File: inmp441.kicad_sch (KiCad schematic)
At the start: 9 parts

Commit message: Revert PWR_FLAG additions - remove '??' squares from schematics
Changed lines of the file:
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@@
-		)
-	)
-	(symbol
-		(lib_id "power:PWR_FLAG")
-		(at 50.0 50.0 0)
-		(unit 1)
-		(body_style 1)
-		(exclude_from_sim no)
-		(in_bom no)
-		(on_board yes)
-		(in_pos_files no)
-		(dnp no)
-		(property "Reference" "#FLG040"
-			(at 50.0 45.0 0)
-			(hide yes)
-			(show_name no)
-			(do_not_autoplace no)
-			(effects
-				(font
-					(size 1.27 1.27)
-				)
-			)
-		)
-		(property "Value" "PWR_FLAG"
-			(at 50.0 55.0 0)
-			(hide yes)
-			(show_name no)
-			(do_not_autoplace no)
-			(effects
-				(font
-					(size 1.27 1.27)
-				)
-			)
-		)
-		(pin "1"
-			(uuid "e3f4a5b6-7890-12cd-ef01-234567890123-pin1")
-		)
-		(instances
-			(project "esp32_xiaozhi"
-				(path "/cae338e8-f342-43cb-b99a-a0486629133c/d2e61921-5974-44e2-9221-de7c05f17e70"
-					(reference "#FLG040")
-					(unit 1)
-				)
-			)
-		)
-	)
-	(symbol
-		(lib_id "power:PWR_FLAG")
-		(at 50.0 100.0 0)
-		(unit 1)
-		(body_style 1)
-		(exclude_from_sim no)
-		(in_bom no)
-		(on_board yes)
-		(in_pos_files no)
-		(dnp no)
-		(property "Reference" "#FLG041"
-			(at 50.0 95.0 0)
-			(hide yes)
-			(show_name no)
-			(do_not_autoplace no)
-			(effects
-				(font
-					(size 1.27 1.27)
-				)
-			)
-		)
-		(property "Value" "PWR_FLAG"
-			(at 50.0 105.0 0)
-			(hide yes)
-			(show_name no)
-			(do_not_autoplace no)
-			(effects
-				(font
-					(size 1.27 1.27)
-				)
-			)
-		)
-		(pin "1"
-			(uuid "e3f4a5b6-7890-12cd-ef01-234567890124-pin1")
-		)
-		(instances
-			(project "esp32_xiaozhi"
-				(path "/cae338e8-f342-43cb-b99a-a0486629133c/d2e61921-5974-44e2-9221-de7c05f17e70"
-					(reference "#FLG041")
-					(unit 1)
-				)
-			)
 		)
 	)

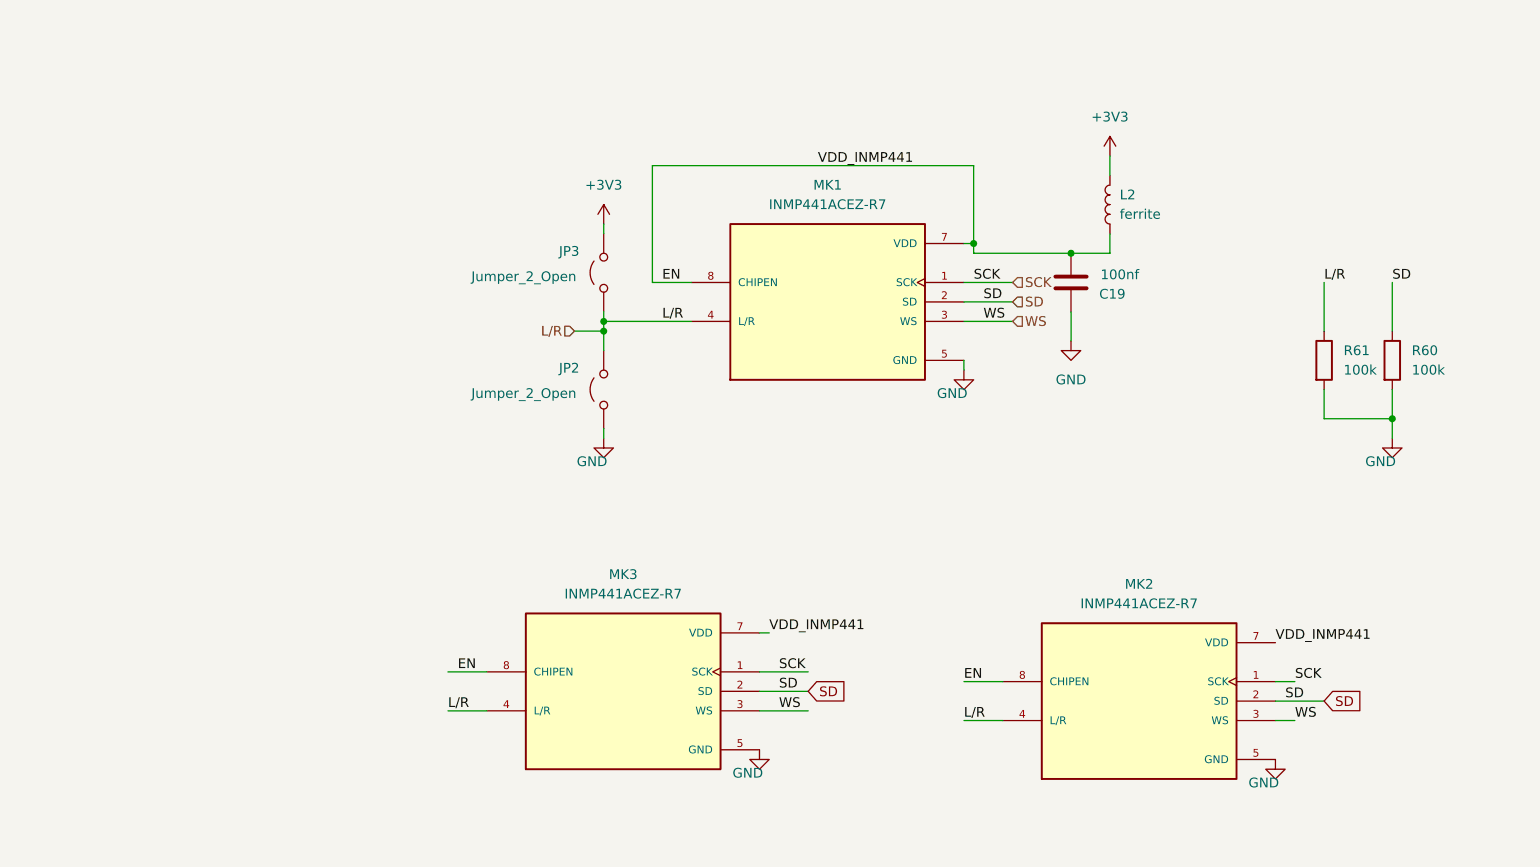
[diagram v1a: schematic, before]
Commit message: Actualización de esquema y PCB del proyecto ESP32C6 Xiaozhi
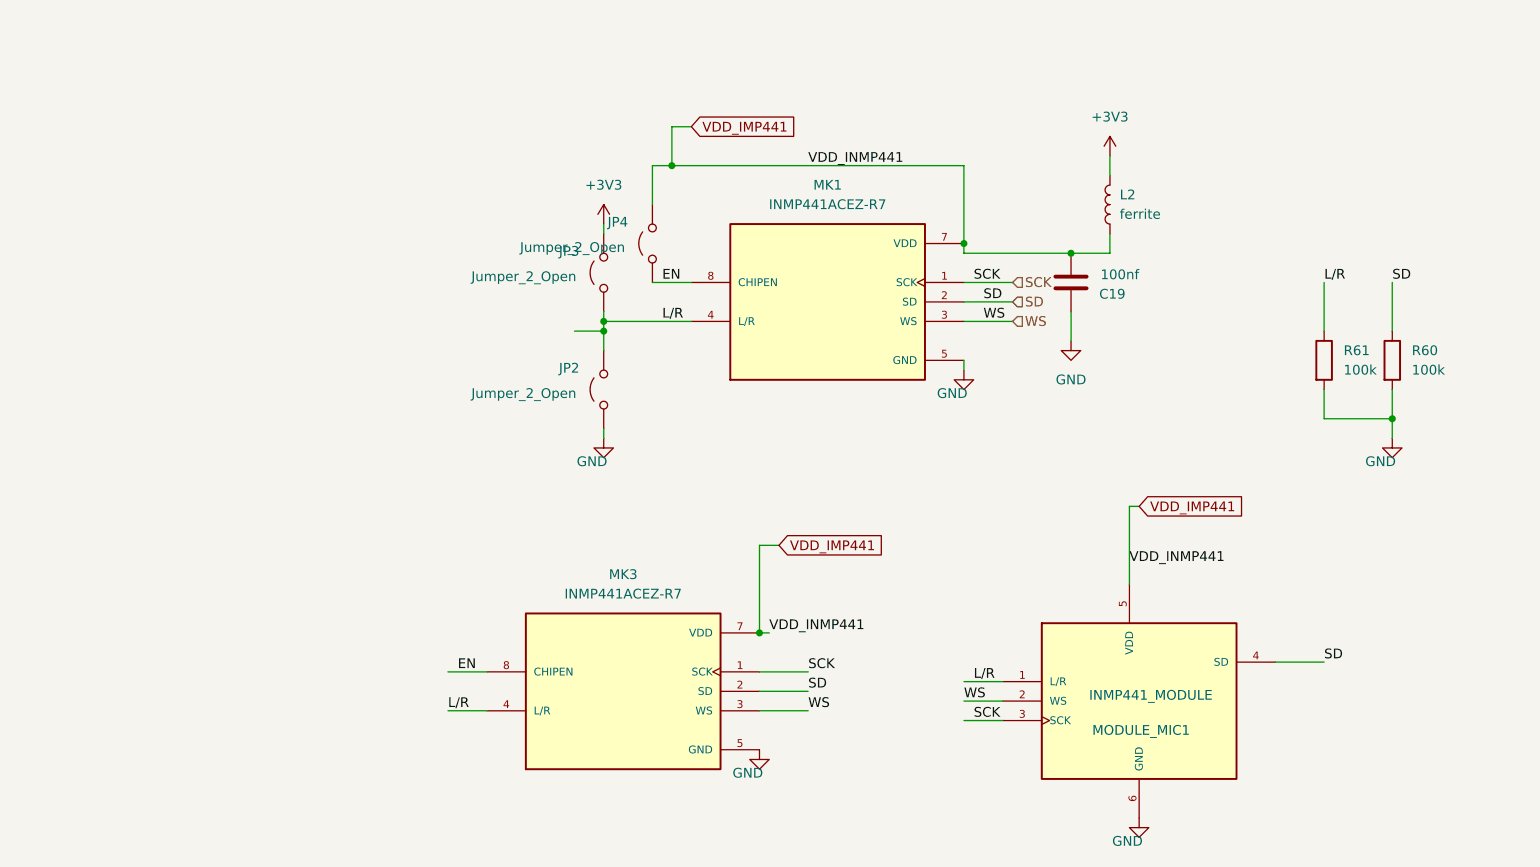
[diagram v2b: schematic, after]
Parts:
- added JP4: Jumper_2_Open, Jumper:SolderJumper-2_P1.3mm_Bridged_RoundedPad1.0x1.5mm, symbol Jumper:Jumper_2_Open
- JP2: footprint Jumper:SolderJumper-2_P1.3mm_Open_RoundedPad1.0x1.5mm -> Jumper:SolderJumper-2_P1.3mm_Bridged_RoundedPad1.0x1.5mm
- L2: footprint Inductor_SMD:L_0805_2012Metric -> Inductor_SMD:L_1206_3216Metric
- MODULE_MIC1: renamed from MK2; value INMP441ACEZ-R7 -> INMP441_MODULE; Check_prices https://www.snapeda.com/parts/INMP441ACEZ-R7/TDK/view-part/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 -> (none); Package LGA-9 TDK InvenSense -> (none); Purchase-URL https://www.snapeda.com/api/url_track_click_mouser/?unipart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 -> (none); SnapEDA_Link https://www.snapeda.com/parts/INMP441ACEZ-R7/TDK/view-part/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 -> (none)
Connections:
- net EN: now also JP4.1 (A); no longer C19.2, L2.1, MK1.7 (VDD), MK3.7 (VDD), MODULE_MIC1.7 (VDD), MODULE_MIC1.8 (CHIPEN)
- net GND: no longer MODULE_MIC1.5 (GND)
- net L/R: now also MODULE_MIC1.1 (L/R); no longer MODULE_MIC1.4 (L/R)
- net SCK: now also MODULE_MIC1.3 (SCK); no longer MODULE_MIC1.1 (SCK)
- net SD: now also MODULE_MIC1.4 (SD); no longer MODULE_MIC1.2 (SD)
- net WS: now also MODULE_MIC1.2 (WS); no longer MODULE_MIC1.3 (WS)
- new net VDD_IMP441: C19.2, JP4.2 (B), L2.1, MK1.7 (VDD), MK3.7 (VDD), MODULE_MIC1.5 (VDD)

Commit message: Update KiCad schematics/PCB and project files
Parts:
- JP2: value Jumper_2_Open -> JP_R
- JP3: value Jumper_2_Open -> JP_L
- JP4: value Jumper_2_Open -> JP_EN
- MK1, MK3: footprint kiC:MIC_INMP441ACEZ-R7 -> kiC:INMP441ACEZ-R7
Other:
- moved on the sheet: C19
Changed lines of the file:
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@@
 	(paper "A4")
 	(junction
-		(at 111.76 76.2)
+		(at 177.8 64.77)
 		(diameter 0)
 		(color 0 0 0 0)
@@
 	)
 	(junction
-		(at 172.72 66.04)
-		(diameter 0)
-		(color 0 0 0 0)
-	)
-	(junction
 		(at 214.63 87.63)
 		(diameter 0)
@@
 	)
 	(junction
+		(at 158.75 64.77)
+		(diameter 0)
+		(color 0 0 0 0)
+	)
+	(junction
 		(at 120.65 54.61)
 		(diameter 0)
 		(color 0 0 0 0)
 	)
-	(junction
-		(at 158.75 64.77)
-		(diameter 0)
-		(color 0 0 0 0)
-	)
 	(wire
 		(pts
@@
 	(wire
 		(pts
-			(xy 107.95 76.2) (xy 111.76 76.2)
-		)
-		(stroke
-			(width 0)
-			(type default)
-		)
-	)
-	(wire
-		(pts
-			(xy 111.76 78.74) (xy 111.76 76.2)
-		)
-		(stroke
-			(width 0)
-			(type default)
-		)
-	)
-	(wire
-		(pts
-			(xy 177.8 66.04) (xy 172.72 66.04)
+			(xy 111.76 74.93) (xy 111.76 78.74)
 		)
 		(stroke
@@
 	(wire
 		(pts
-			(xy 158.75 64.77) (xy 158.75 66.04)
-		)
-		(stroke
-			(width 0)
-			(type default)
-		)
-	)
-	(wire
-		(pts
 			(xy 91.44 120.65) (xy 96.52 120.65)
 		)
@@
 	(wire
 		(pts
-			(xy 172.72 73.66) (xy 172.72 77.47)
-		)
-		(stroke
-			(width 0)
-			(type default)
-		)
-	)
-	(wire
-		(pts
 			(xy 132.08 104.14) (xy 132.08 115.57)
 		)
@@
 	(wire
 		(pts
-			(xy 111.76 74.93) (xy 111.76 76.2)
-		)
-		(stroke
-			(width 0)
-			(type default)
-		)
-	)
-	(wire
-		(pts
 			(xy 118.11 69.85) (xy 123.19 69.85)
 		)
@@
 	(wire
 		(pts
-			(xy 177.8 63.5) (xy 177.8 66.04)
-		)
-		(stroke
-			(width 0)
-			(type default)
-		)
-	)
-	(wire
-		(pts
-			(xy 158.75 66.04) (xy 172.72 66.04)
+			(xy 177.8 63.5) (xy 177.8 64.77)
+		)
+		(stroke
+			(width 0)
+			(type default)
+		)
+	)
+	(wire
+		(pts
+			(xy 158.75 64.77) (xy 177.8 64.77)
 		)
 		(stroke
@@
 	(wire
 		(pts
+			(xy 177.8 64.77) (xy 177.8 66.04)
+		)
+		(stroke
+			(width 0)
+			(type default)
+		)
+	)
+	(wire
+		(pts
 			(xy 111.76 62.23) (xy 111.76 63.5)
 		)
@@
 		(pts
 			(xy 158.75 127) (xy 163.83 127)
+		)
+		(stroke
+			(width 0)
+			(type default)
+		)
+	)
+	(wire
+		(pts
+			(xy 177.8 73.66) (xy 177.8 77.47)
 		)
 		(stroke
@@
 			)
 		)
-		(property "Footprint" "kiC:MIC_INMP441ACEZ-R7"
+		(property "Footprint" "kiC:INMP441ACEZ-R7"
 			(at 114.3 123.19 0)
 			(hide yes)
@@
 			)
 		)
-		(property "Value" "Jumper_2_Open"
-			(at 94.488 84.328 90)
+		(property "Value" "JP_R"
+			(at 112.522 84.074 90)
 			(show_name no)
 			(do_not_autoplace no)
@@
 	(symbol
 		(lib_id "power:GND")
-		(at 172.72 77.47 0)
+		(at 177.8 77.47 0)
 		(unit 1)
 		(body_style 1)
@@
 		(fields_autoplaced yes)
 		(property "Reference" "#PWR040"
-			(at 172.72 83.82 0)
+			(at 177.8 83.82 0)
 			(hide yes)
 			(show_name no)
@@
 		)
 		(property "Value" "GND"
-			(at 172.72 82.55 0)
+			(at 177.8 82.55 0)
 			(show_name no)
 			(do_not_autoplace no)
@@
 		)
 		(property "Footprint" ""
-			(at 172.72 77.47 0)
+			(at 177.8 77.47 0)
 			(hide yes)
 			(show_name no)
@@
 		)
 		(property "Datasheet" ""
-			(at 172.72 77.47 0)
+			(at 177.8 77.47 0)
 			(hide yes)
 			(show_name no)
@@
 		)
 		(property "Description" ""
-			(at 172.72 77.47 0)
+			(at 177.8 77.47 0)
 			(show_name no)
 			(do_not_autoplace no)
@@
 			)
 		)
-		(property "Value" "Jumper_2_Open"
-			(at 100.838 65.278 90)
+		(property "Value" "JP_EN"
+			(at 116.84 42.418 0)
 			(show_name no)
 			(do_not_autoplace no)
@@
 	(symbol
 		(lib_id "Device:C")
-		(at 172.72 69.85 180)
+		(at 177.8 69.85 180)
 		(unit 1)
 		(body_style 1)
@@
 		(dnp no)
 		(property "Reference" "C19"
-			(at 179.832 71.374 0)
+			(at 184.912 71.374 0)
 			(show_name no)
 			(do_not_autoplace no)
@@
 		)
 		(property "Value" "100nf"
-			(at 181.61 68.834 0)
+			(at 186.69 68.834 0)
 			(show_name no)
 			(do_not_autoplace no)
@@
 		)
 		(property "Footprint" "Capacitor_SMD:C_0805_2012Metric"
-			(at 171.7548 66.04 0)
+			(at 176.8348 66.04 0)
 			(hide yes)
 			(show_name no)
@@
 		)
 		(property "Datasheet" ""
-			(at 172.72 69.85 0)
+			(at 177.8 69.85 0)
 			(hide yes)
 			(show_name no)
@@
 		)
 		(property "Description" ""
-			(at 172.72 69.85 0)
+			(at 177.8 69.85 0)
 			(show_name no)
 			(do_not_autoplace no)
@@
 			)
 		)
-		(property "Value" "Jumper_2_Open"
-			(at 94.488 69.088 90)
+		(property "Value" "JP_L"
+			(at 105.41 69.088 90)
 			(show_name no)
 			(do_not_autoplace no)
@@
 			)
 		)
-		(property "Footprint" "kiC:MIC_INMP441ACEZ-R7"
+		(property "Footprint" "kiC:INMP441ACEZ-R7"
 			(at 140.97 72.39 0)
 			(hide yes)

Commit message: add files update
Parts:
- MK1, MK3, MODULE_MIC1: now left out of the parts list
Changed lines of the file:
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@@
 		(body_style 1)
 		(exclude_from_sim no)
-		(in_bom yes)
-		(on_board yes)
-		(in_pos_files yes)
+		(in_bom no)
+		(on_board yes)
+		(in_pos_files no)
 		(dnp no)
 		(fields_autoplaced yes)
@@
 		(body_style 1)
 		(exclude_from_sim no)
-		(in_bom yes)
-		(on_board yes)
-		(in_pos_files yes)
+		(in_bom no)
+		(on_board yes)
+		(in_pos_files no)
 		(dnp no)
 		(fields_autoplaced yes)
@@
 		(body_style 1)
 		(exclude_from_sim no)
-		(in_bom yes)
-		(on_board yes)
-		(in_pos_files yes)
+		(in_bom no)
+		(on_board yes)
+		(in_pos_files no)
 		(dnp no)
 		(fields_autoplaced yes)

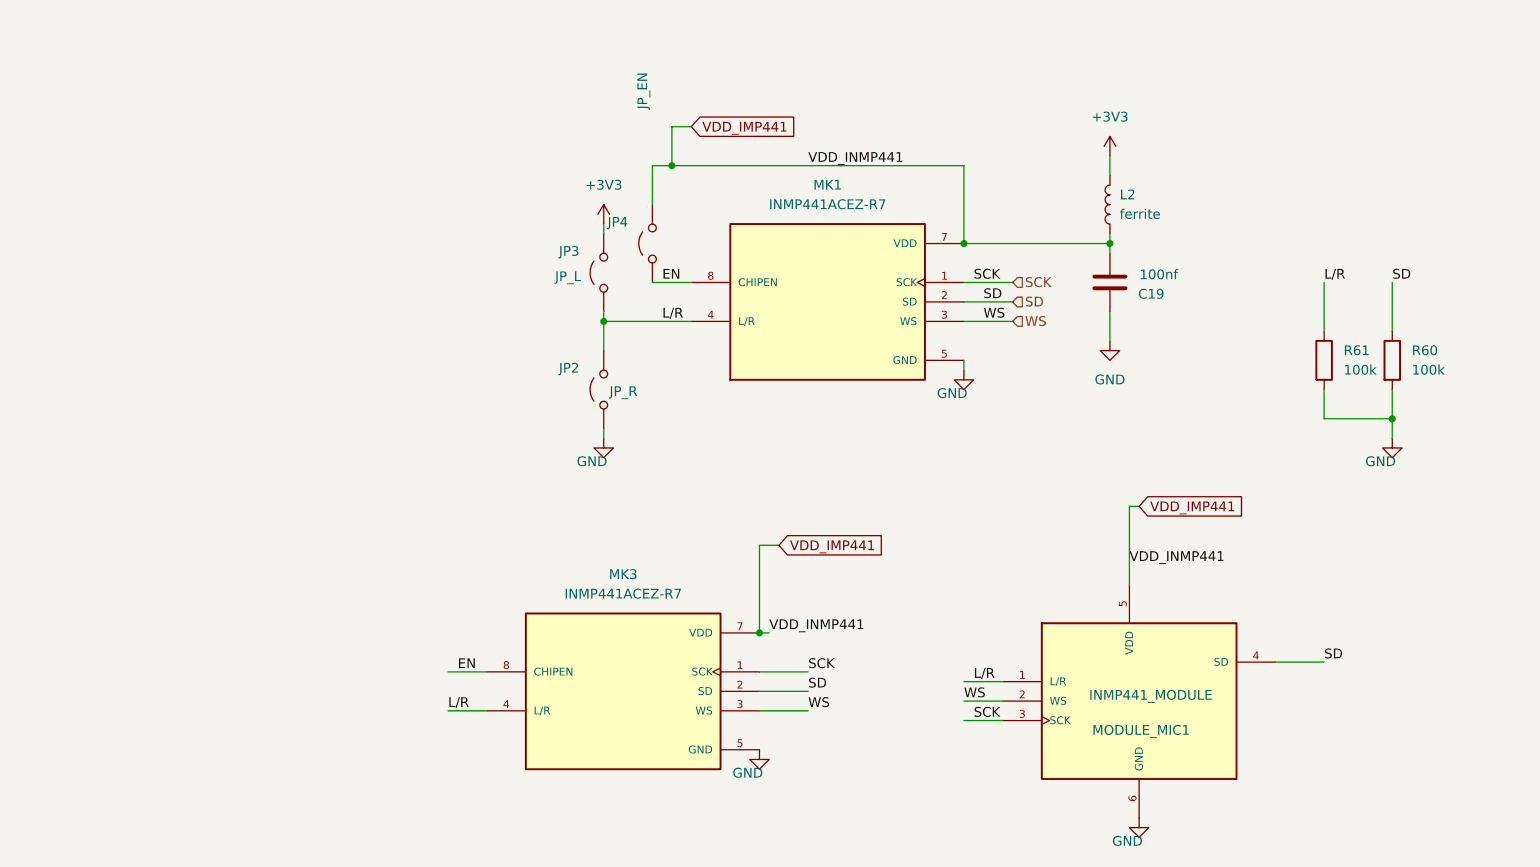
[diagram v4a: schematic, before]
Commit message: Actualización de esquemas y PCB con datos LCSC y librerías JLC
- Añade propiedades LCSC a los símbolos de las hojas de esquema
- Actualiza las hojas TXS0108E, display, esp32_c6, ft232, inmp441,
  led_sw_gpio, max98357a, micro_sd, power_supply y el esquema raíz
- Reorganiza el PCB (footprints, jumpers y nets) y actualiza el proyecto
- Incluye las librerías locales JLCImport (símbolos, huellas y modelos 3D)
  y las entradas correspondientes en fp-lib-table y sym-lib-table
- Añade la documentación técnica en docs/ y el archivo de posiciones
  esp32_xiaozhi-all.pos
- Elimina los ZIP generados gebers.zip y production.zip
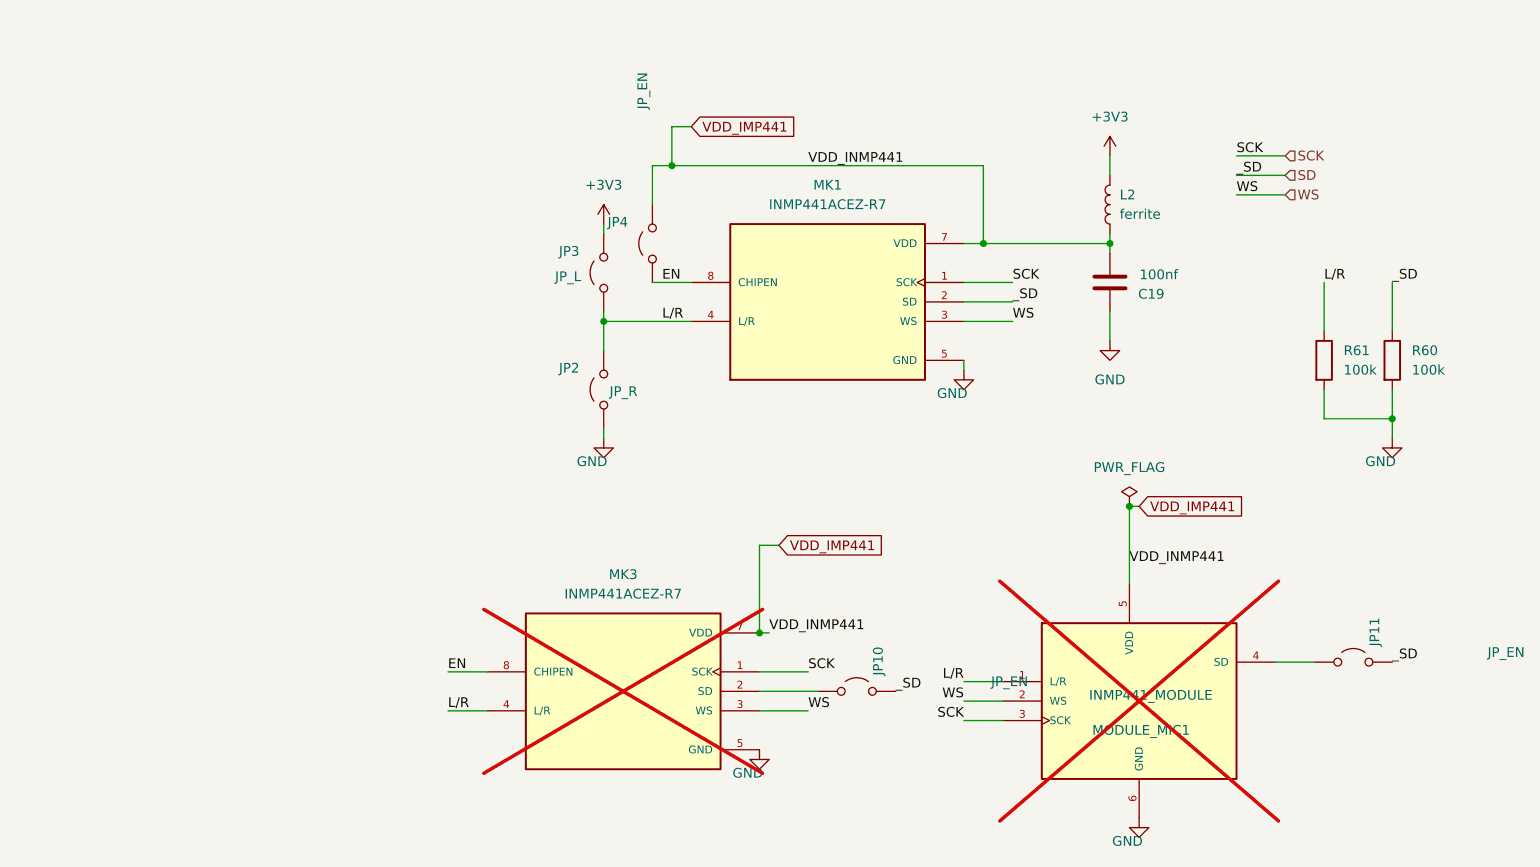
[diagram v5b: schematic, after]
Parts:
- added JP10, JP11: JP_EN, Jumper:SolderJumper-2_P1.3mm_Open_RoundedPad1.0x1.5mm, symbol Jumper:Jumper_2_Open
- C19: LCSC (none) -> C1525
- JP2, JP3, JP4: now left out of the parts list
- L2: LCSC (none) -> C74489
- MK1: LCSC (none) -> C5438445; now in the parts list
- MK3, MODULE_MIC1: LCSC (none) -> C5438445; now not fitted
- R60, R61: LCSC (none) -> C149504
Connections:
- net SD: now also JP10.2 (B), JP11.2 (B); no longer MK3.2 (SD), MODULE_MIC1.4 (SD)
- new net: JP10.1 (A), MK3.2 (SD)
- new net: JP11.1 (A), MODULE_MIC1.4 (SD)

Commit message: Actualización de esquemas, PCB y librerías
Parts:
- C19: LCSC C1525 -> C28233
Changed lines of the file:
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@@
 			)
 		)
-		(property "LCSC" "C1525"
+		(property "LCSC" "C28233"
 			(at 177.8 69.85 0)
 			(hide yes)

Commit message: update files
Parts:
- MK1: LCSC C5438445 -> C22379536
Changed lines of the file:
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@@
 			)
 		)
-		(property "LCSC" "C5438445"
+		(property "LCSC" "C22379536"
 			(at 140.97 72.39 0)
 			(hide yes)

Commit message: actualizacion  de pcb logic , rpi
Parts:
- MK1, MK3: Package LGA-9 TDK InvenSense -> (none)
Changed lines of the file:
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@@
-			)
-		)
-		(property "Package" "LGA-9 TDK InvenSense"
-			(at 114.3 123.19 0)
-			(hide yes)
-			(show_name no)
-			(do_not_autoplace no)
-			(effects
-				(font
-					(size 1.27 1.27)
-				)
-				(justify bottom)
 			)
 		)
@@
 			)
 		)
-		(property "Package" ""
-			(at 181.61 124.46 0)
-			(hide yes)
-			(show_name no)
-			(do_not_autoplace no)
-			(effects
-				(font
-					(size 1.27 1.27)
-				)
-				(justify bottom)
-			)
-		)
 		(property "Price" "None"
 			(at 197.612 114.046 0)
@@
 			(at 140.97 72.39 0)
 			(hide yes)
-			(show_name no)
-			(do_not_autoplace no)
-			(effects
-				(font
-					(size 1.27 1.27)
-				)
-				(justify bottom)
-			)
-		)
-		(property "Package" "LGA-9 TDK InvenSense"
-			(at 140.97 72.39 0)
-			(hide yes)
